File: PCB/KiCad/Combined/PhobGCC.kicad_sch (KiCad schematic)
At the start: 66 parts, among them J1 Conn_01x06_Female, J2 Conn_01x04_Female, J3 Conn_01x01_Male, J5 Conn_01x02_Male, Q1 Q_NMOS_GSD, Q2 Q_PMOS_GDS, Q3 Q_NMOS_GSD, SW1 A, SW10 Dup, SW11 Dright, SW12 Ddown, SW2 B, SW3 X, SW4 Y, SW5 Start, SW6 L, SW7 R, SW9 Dleft, U1 Teensy4.0, U2 2x DRV5053CAQLPGM Hall Effect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, U3 GP2S60-MFG, U4 GP2S60-MFG

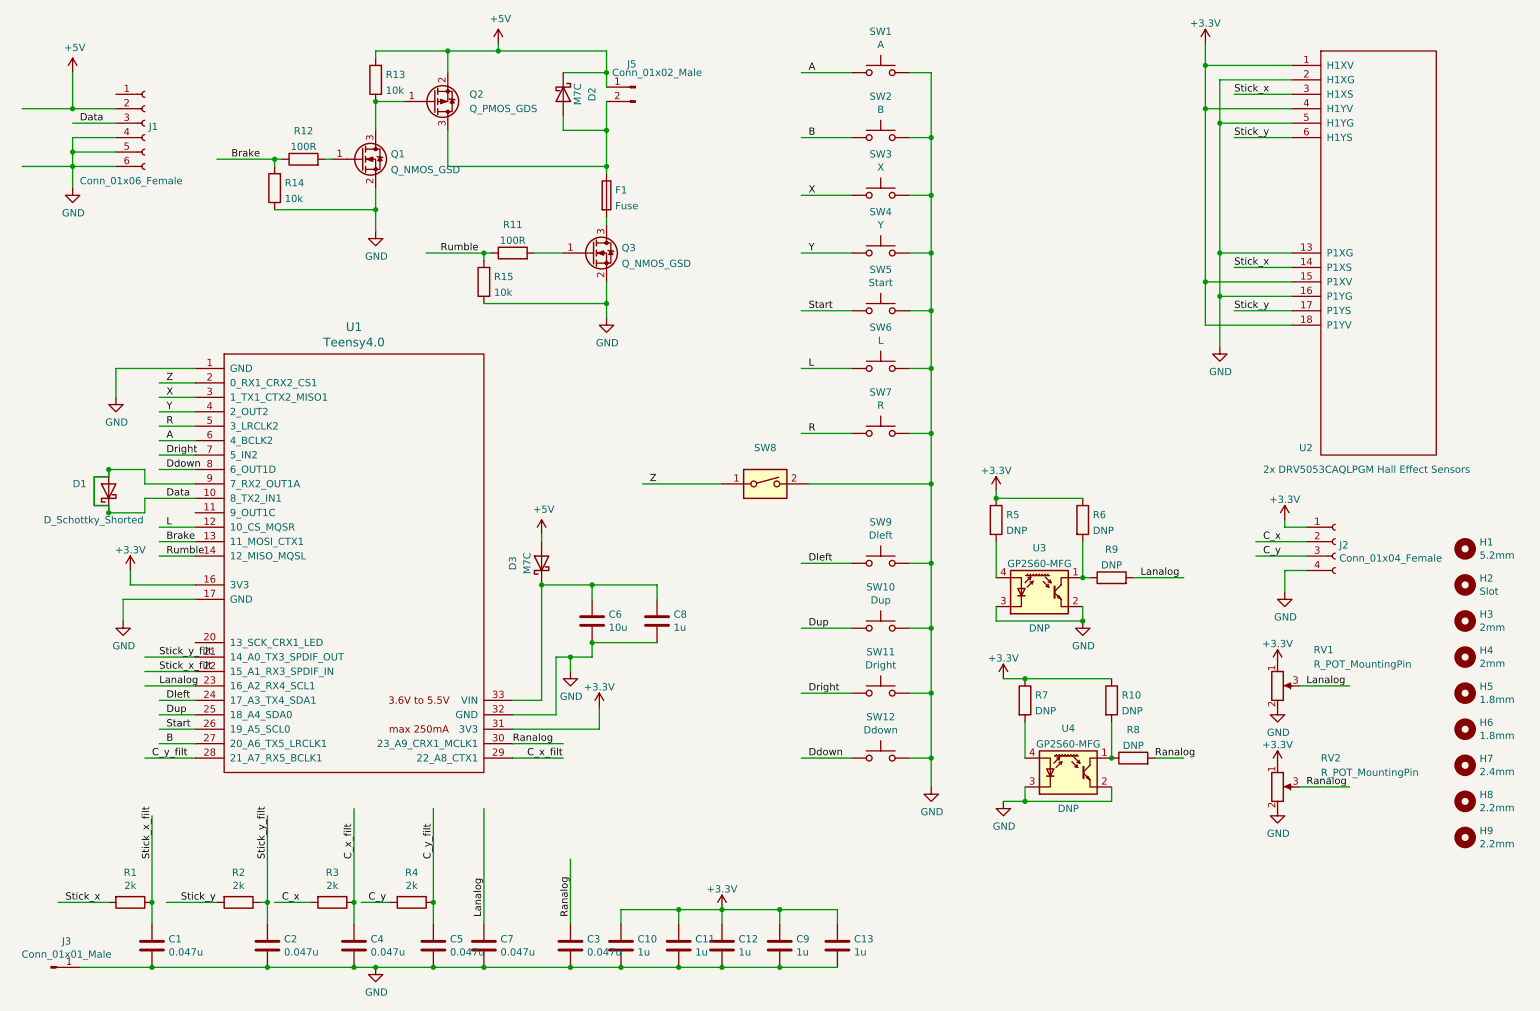
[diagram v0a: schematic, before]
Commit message: Updates
- switched rumble pads to SMD and matched OEM placement.
- aligned both sets of trigger pads to be horizontal for convenience and consistency.
- centered c-stick pins to the board edge.
- rerouted some areas to have a more consistent copper fill.
- fixed trigger board width (switched 7.5mm to 7.35mm).
- increased dpad button pad size to make for easier hand soldering.
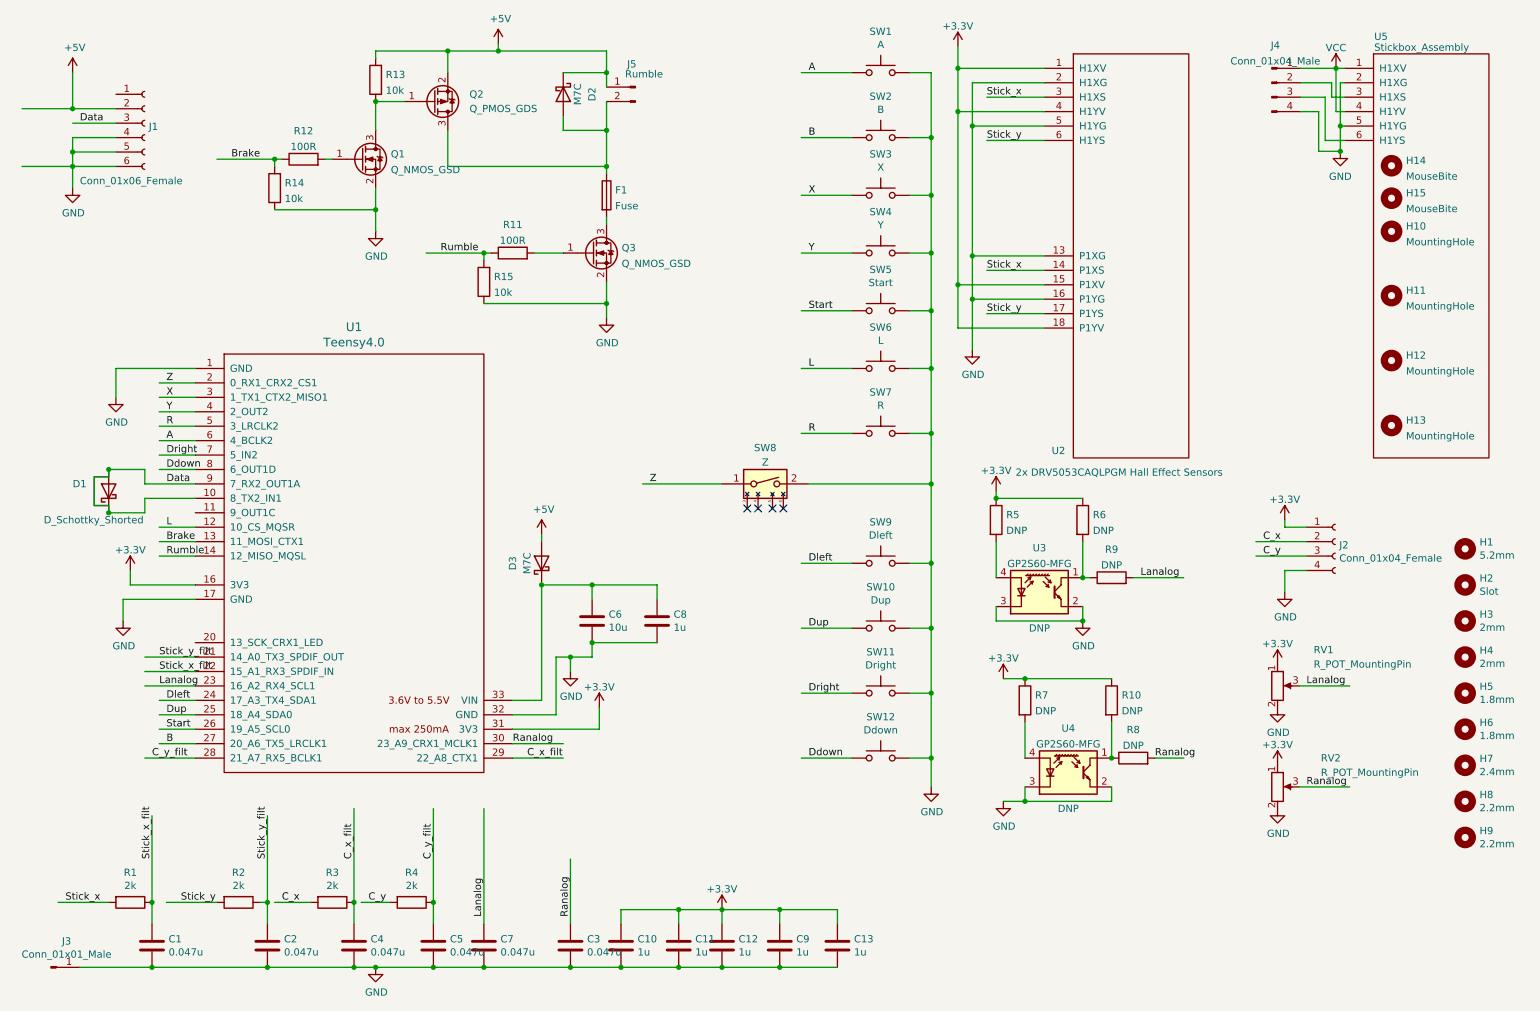
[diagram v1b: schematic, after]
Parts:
- added H10: MountingHole, PhobGCC_Footprints:MountingHole_1.8mm, symbol Mechanical:MountingHole
- added H11: MountingHole, PhobGCC_Footprints:MountingHole_5.2mm, symbol Mechanical:MountingHole
- added H12, H13: MountingHole, PhobGCC_Footprints:MountingHole_2.0mm, symbol Mechanical:MountingHole
- added H14, H15: MouseBite, PhobGCC_Footprints:breakaway-mousebites-double, symbol Mechanical:MountingHole
- added J4: Conn_01x04_Male, Connector_PinHeader_2.00mm:PinHeader_1x04_P2.00mm_Vertical, symbol Connector:Conn_01x04_Male
- added U5: Stickbox_Assembly, PhobGCC_Footprints:GCC_Stickbox_Hall_Only, symbol Gamecube MB:Stickbox_Assembly_Hall_Only
- J5: value Conn_01x02_Male -> Rumble; footprint PhobGCC_Footprints:Pin_Header_Straight_1x02_Pitch2.54mm -> PhobGCC_Footprints:rumble_pins
- SW10, SW11, SW12, SW9: footprint PhobGCC_Footprints:Dpad_Contact_TL3315NF_2 -> (none)
- SW8: value (none) -> Z; symbol Switch:SW_DIP_x01 -> PhobGCC_Symbol_Library:SW_DIP_x01
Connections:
- net GND: now also J4.4 (Pin_4), U5.2 (H1XG), U5.5 (H1YG)
- new net: J4.2 (Pin_2), U5.3 (H1XS)
- new net: J4.3 (Pin_3), U5.6 (H1YS)
- new net VCC: J4.1 (Pin_1), U5.1 (H1XV), U5.4 (H1YV)
- no-connect marks 0 -> 4
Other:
- moved on the sheet: U2

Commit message: Consolidated footprints to PhobGCC library
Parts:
- C1, C2, C3, C4, C5, C6, C7: footprint Capacitors_SMD:C_0603_HandSoldering -> PhobGCC_Footprints:C_0603_HandSoldering
- C10, C11, C12, C13, C8, C9: footprint Capacitor_SMD:C_0603_1608Metric_Pad1.08x0.95mm_HandSolder -> PhobGCC_Footprints:C_0603_1608Metric_Pad1.08x0.95mm_HandSolder
- D2, D3: footprint Diode_SMD:D_SOD-123 -> PhobGCC_Footprints:D_SOD-123
- F1: footprint Resistor_SMD:R_1206_3216Metric -> PhobGCC_Footprints:Fuse_1206_3216Metric
- J2: footprint Pin_Headers:Pin_Header_Straight_1x04_Pitch2.00mm -> PhobGCC_Footprints:PinHeader_1x04_P2.00mm_Vertical
- J3: footprint Connector_PinHeader_2.54mm:PinHeader_1x01_P2.54mm_Vertical -> PhobGCC_Footprints:PinHeader_1x01_P2.54mm_Vertical
- J4: footprint Connector_PinHeader_2.00mm:PinHeader_1x04_P2.00mm_Vertical -> PhobGCC_Footprints:PinHeader_1x04_P2.00mm_Vertical
- Q1, Q2, Q3: footprint Package_TO_SOT_SMD:SOT-23 -> PhobGCC_Footprints:SOT-23
- R1, R11, R12, R13, R14, R15, R2, R3, R4: footprint Resistor_SMD:R_0603_1608Metric_Pad0.98x0.95mm_HandSolder -> PhobGCC_Footprints:R_0603_1608Metric_Pad0.98x0.95mm_HandSolder
- R10, R5, R6, R7, R8, R9: footprint Resistor_SMD:R_0603_1608Metric_Pad0.98x0.95mm_HandSolder -> PhobGCC_Footprints:R_0603_1608_DNP
- SW10, SW11, SW12, SW9: footprint (none) -> PhobGCC_Footprints:Dpad_Contact_TL3315NF_2

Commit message: 1.2.3 changes
omron tactile z support, larger c stick pin holes, relocated C10 from underneath button pad
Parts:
- SW8: footprint PhobGCC_Footprints:Z_Switch_Edge -> (none)
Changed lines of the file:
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@@
     (property "Reference" "SW8" (id 0) (at 148.59 88.9 0))
     (property "Value" "Z" (id 1) (at 148.59 91.44 0))
-    (property "Footprint" "PhobGCC_Footprints:Z_Switch_Edge" (id 2) (at 148.59 95.25 0)
+    (property "Footprint" "" (id 2) (at 148.59 95.25 0)
       (effects (font (size 1.27 1.27)) hide)
     )
@@
     )
     (path "/00000000-0000-0000-0000-00006159dc5a"
-      (reference "SW8") (unit 1) (value "Z") (footprint "PhobGCC_Footprints:Z_Switch_Edge")
+      (reference "SW8") (unit 1) (value "Z") (footprint "PhobGCC_Footprints:Z_Switch_Edge_Omron")
     )
     (path "/00000000-0000-0000-0000-00006157aadd"
